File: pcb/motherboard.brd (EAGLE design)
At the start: 80.6 x 51.4 mm, 49 parts

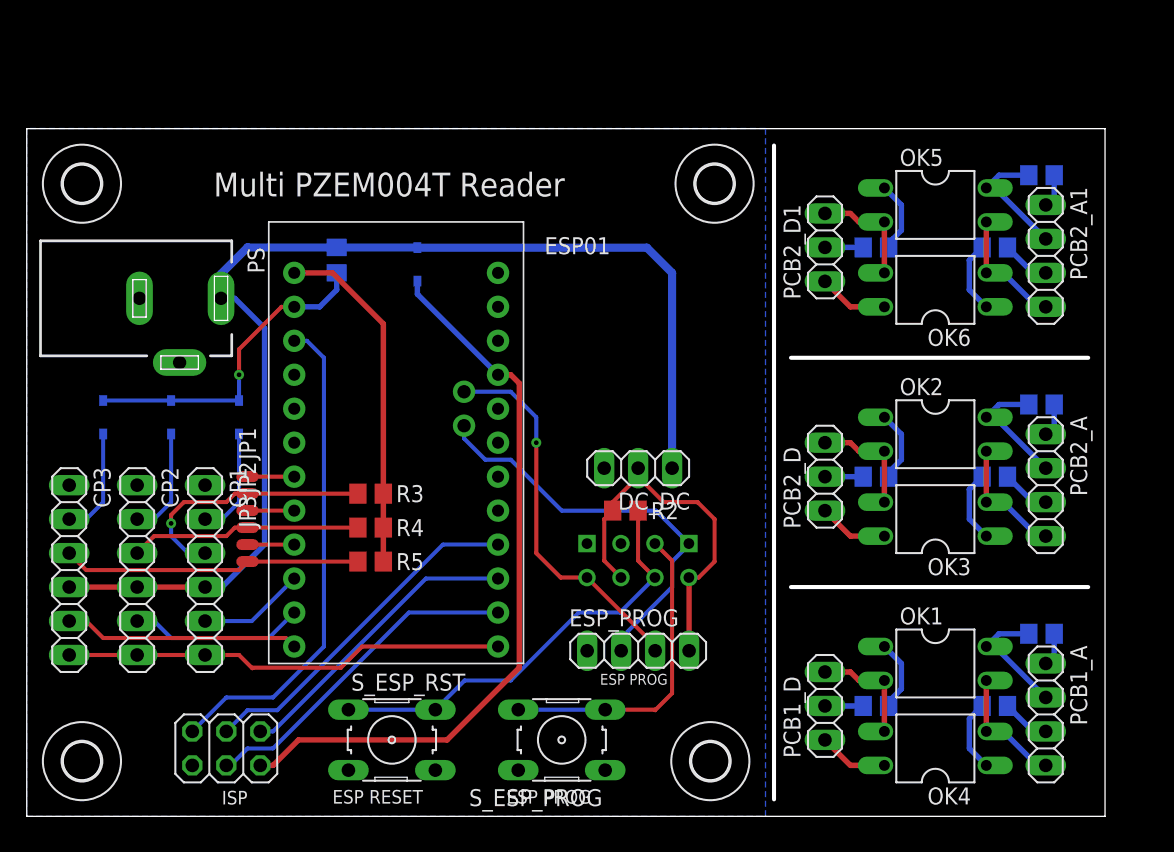
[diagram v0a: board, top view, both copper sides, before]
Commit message: Modified to support 6 devices.
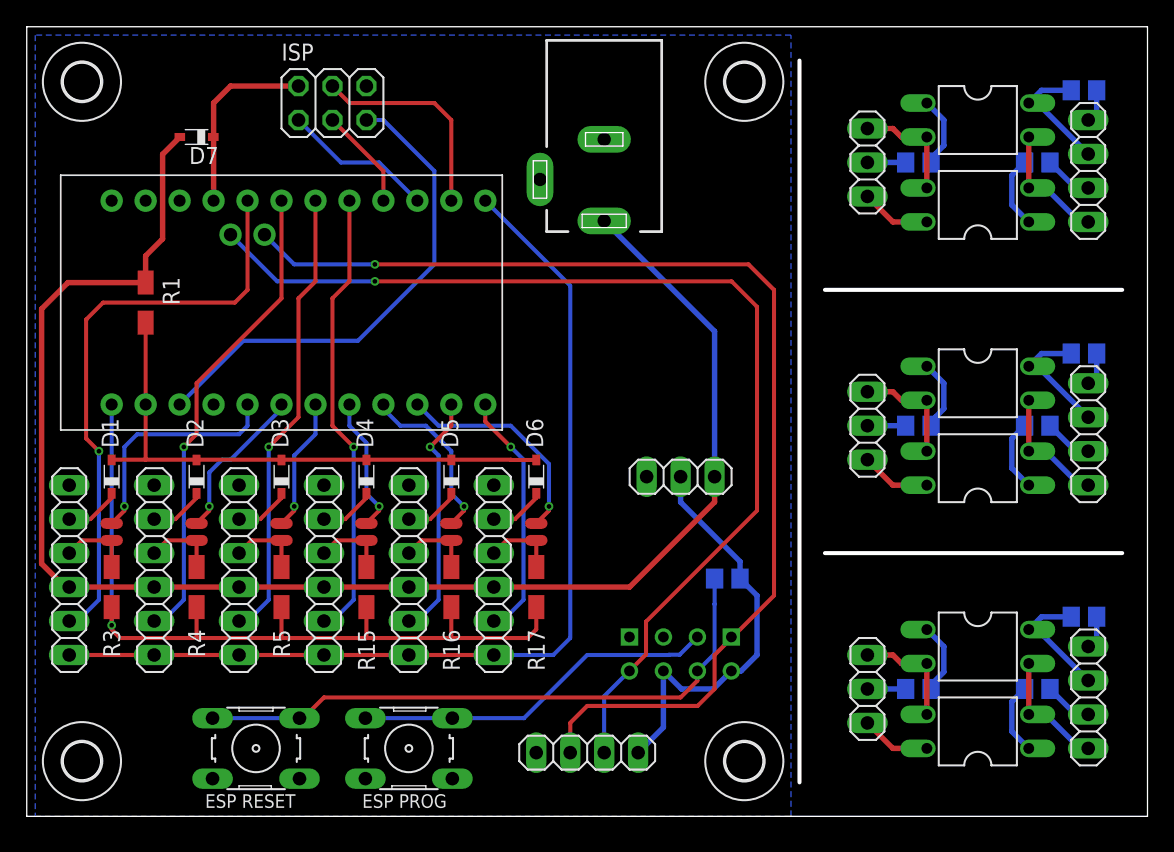
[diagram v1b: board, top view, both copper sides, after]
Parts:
- added CP4, CP5, CP6: (no value), pinhead:1X06
- added D5, D6, D7: BAT43, diode:SOD323_ST
- added JP4, JP5, JP6: SMD_JUMPER, EPIC:SMD_JUMPER
- added R15, R16, R17: 10K, resistor:R1206W
- R1, R3, R4, R5: device resistor:R0805 -> resistor:R1206W
- moved ISP 48.9 mm to (22.9, 53.3), turned to 0 degrees
- moved PS 33.0 mm to (43.2, 47.6), turned to 180 degrees
- moved R3 20.6 mm to (6.35, 17.1), turned to 270 degrees
- moved D4 16.3 mm to (25.4, 25.4), flipped to the top
- moved R1 14.6 mm to (8.89, 38.4), flipped to the top
- moved D3 14.1 mm to (19.1, 25.4), flipped to the top
- moved R4 13.8 mm to (12.7, 17.1), turned to 270 degrees
- moved MEGAPRO 13.5 mm to (19.1, 38.4), turned to 90 degrees
- moved CP3 12.7 mm to (15.9, 18.4)
- moved S_ESP_PROG 11.4 mm to (28.6, 5.08)
- moved JP1 10.7 mm to (6.35, 21.3)
- moved D1 10.5 mm to (6.35, 25.4), flipped to the top
- moved S_ESP_RST 10.2 mm to (17.1, 5.08)
- moved CP1 10.2 mm to (3.17, 18.4)
- moved GOLD_ORB_SM1 9.21 mm to (35.6, 39.4)
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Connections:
- new net DIR4: CP4.5, MEGAPRO.17
- new net DIR5: CP5.5, MEGAPRO.11
- new net DIR6: CP6.5, MEGAPRO.12
- new net N$10: CP5.3, JP5.P0, R16.1
- new net N$11: CP6.3, JP6.P0, R17.1
- new net N$9: CP4.3, JP4.P0, R15.1
- new net RX4: CP4.2, D4.C
- new net RX5: CP5.2, D5.C
- new net RX6: CP6.2, D6.C
- new net _TX4_EN: JP4.P1, MEGAPRO.8
- new net _TX5_EN: JP5.P1, MEGAPRO.9
- new net _TX6_EN: JP6.P1, MEGAPRO.10
- net DIR1: now also MEGAPRO.20; no longer MEGAPRO.10
- net DIR2: now also MEGAPRO.19; no longer MEGAPRO.11
- net DIR3: now also MEGAPRO.18; no longer MEGAPRO.12
- net GND: now also CP4.1, CP5.1, CP6.1
- net ISP_VCC: now also D7.C; no longer D4.C
- net PZ_RST: now also CP4.6, CP5.6, CP6.6
- net RX: now also D4.A, D5.A, D6.A
- net TX: now also R15.2, R16.2, R17.2
- net VCC: now also CP4.4, CP5.4, CP6.4, D7.A; no longer D4.A
- net _TX1_EN: now also MEGAPRO.5; no longer MEGAPRO.7
- net _TX2_EN: now also MEGAPRO.6; no longer MEGAPRO.8
- net _TX3_EN: now also MEGAPRO.7; no longer MEGAPRO.9
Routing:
- net SDA_ESP_RX: track 31.1 -> 85.7 mm, vias 0 -> 1
- net SCL_ESP_TX: track 28.5 -> 79.7 mm
- net ISP_VCC: track 55.0 -> 14.2 mm
- net PZ_RST: track 33.2 -> 73.3 mm
- net DIR1: track 7.98 -> 43.9 mm, vias 0 -> 1
- net TX: track 26.0 -> 61.4 mm, vias 0 -> 1
- net DIR4: track 0.00 -> 33.9 mm, vias 0 -> 1
- net VCC: track 88.1 -> 117.7 mm
- net DIR2: track 13.1 -> 35.7 mm, vias 0 -> 1
- net DIR6: track 0.00 -> 18.7 mm, vias 0 -> 1
- net SCK: track 26.1 -> 7.61 mm
- net DIR5: track 0.00 -> 18.4 mm, vias 0 -> 1
- net RX: track 24.4 -> 42.4 mm, vias 1 -> 0
- net N$4: track 22.4 -> 5.56 mm
- net DIR3: track 17.6 -> 34.2 mm, vias 0 -> 1
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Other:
- board size 80.6 x 51.4 mm -> 83.8 x 59 mm
- board text added: "3.3V"
- board text added: "CH/PD"
- board text added: "CH1"
- board text added: "CH2"
- board text added: "CH3"
- board text added: "CH4"
- board text added: "CH5"
- board text added: "CH6"
- board text added: "ESP ISP"
- board text added: "GPIO0"
- board text added: "GPIO2"
- board text added: "RX"
- board text added: "Rev. 1"
- board text added: "TX"

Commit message: Updated PCB/Schematic.
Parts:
- moved D7 8.64 mm to (10.2, 42.5)
- moved GOLD_ORB_SM1 1.27 mm to (34.3, 39.4)
- moved R1 0.63 mm to (8.89, 37.8)
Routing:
- net VCC: track 117.7 -> 109.2 mm
- net ISP_VCC: track 14.2 -> 19.1 mm
- net RX: track 42.4 -> 41.5 mm
- net SDA_ESP_RX: track 85.7 -> 86.4 mm
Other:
- board text added: "High Voltage"
